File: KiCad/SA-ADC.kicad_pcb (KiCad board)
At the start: 4 copper layers, 99.1 x 94.2 mm, 226 parts, among them J1 Conn_01x03, J2 Conn_01x02, J3 Conn_01x08, SW1 SW_Push_SPDT, SW2 SW_Push, U1 40193, U10 74LVC1G32, U11 74LVC1G32, U12 74LVC1G32, U13 74LS21, U14 74LS21, U15 74LS21, U16 74LS21, U17 74LS21, U18 74AHC1G08, U19 74AHC1G08, U2 40193, U20 74LS21, U21 74AHC1G08, U22 74AHC1G08, U23 74LS21, U24 74LS21, U25 74AHC1G08, U26 74AHC1G08, U27 74AHC1G08, U28 74AHC1G08, U29 74LS21, U3 74HC04, U30 74LS21, U31 74AHC1G08, U32 74AHC1G08, U33 74AHC1G08, U34 LM358, U35 74LVC1G125, U36 74HC74, U37 LM317L_TO92, U38 L7805, U39 74HC74, U4 40245, U40 74HC74, U41 74HC74, U42 74LVC1G14, U43 74LS574, U44 LM555, U45 74LVC1G125, U46 74AHC1G08, U47 74LVC1G32, U48 74LVC1G125, U5 74LVC1G32, U6 74LVC1G32, U7 74LVC1G32, U8 74LVC1G32, U9 74LVC1G32

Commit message: Removed version nums
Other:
- board text added: "[version]"
- board text removed: "v0.0"
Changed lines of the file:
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@@
   (title_block
     (title SA-ADC)
-    (date 2020-02-13)
-    (rev "v0.0 (Prod.)")
   )
   (layers
@@
     (effects (font (size 2 2) (thickness 0.2)))
   )
-  (gr_text v0.0 (at 190.5 138.43) (layer B.SilkS)
+  (gr_text [version] (at 189.23 138.43) (layer B.SilkS)
     (effects (font (size 1 1) (thickness 0.15)) (justify mirror))
   )

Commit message: Fixed netlist-conformity due to renamed schematic sheet.
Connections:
- net /OutputDisplay/OUT_0 renamed Net-(J3-Pad1)
- net /OutputDisplay/OUT_1 renamed Net-(J3-Pad2)
- net /OutputDisplay/OUT_2 renamed Net-(J3-Pad3)
- net /OutputDisplay/OUT_3 renamed Net-(J3-Pad4)
- net /OutputDisplay/OUT_4 renamed Net-(J3-Pad5)
- net /OutputDisplay/OUT_5 renamed Net-(J3-Pad6)
- net /OutputDisplay/OUT_6 renamed Net-(J3-Pad7)
- net /OutputDisplay/OUT_7 renamed Net-(J3-Pad8)
- net /Registers.sch/Latch0 renamed /SA-Register.sch/Latch0
- net /Registers.sch/Latch1 renamed /SA-Register.sch/Latch1
- net /Registers.sch/Latch2 renamed /SA-Register.sch/Latch2
- net /Registers.sch/Latch3 renamed /SA-Register.sch/Latch3
- net /Registers.sch/Latch4 renamed /SA-Register.sch/Latch4
- net /Registers.sch/Latch5 renamed /SA-Register.sch/Latch5
- net /Registers.sch/Latch6 renamed /SA-Register.sch/Latch6
- net /Registers.sch/Latch7 renamed /SA-Register.sch/Latch7
- net /Registers.sch/LatchOutput renamed /Output/LatchOutput
- net /Registers.sch/Q0 renamed /Output/OUT_0
- net /Registers.sch/Q1 renamed /Output/OUT_1
- net /Registers.sch/Q2 renamed /Output/OUT_2
- net /Registers.sch/Q3 renamed /Output/OUT_3
- net /Registers.sch/Q4 renamed /Output/OUT_4
- net /Registers.sch/Q5 renamed /Output/OUT_5
- net /Registers.sch/Q6 renamed /Output/OUT_6
- net /Registers.sch/Q7 renamed /Output/OUT_7
- net /Registers.sch/Reset renamed /SA-Register.sch/Reset
- net /Registers.sch/Test0 renamed /SA-Register.sch/Test0
- net /Registers.sch/Test1 renamed /SA-Register.sch/Test1
- net /Registers.sch/Test2 renamed /SA-Register.sch/Test2
- net /Registers.sch/Test3 renamed /SA-Register.sch/Test3
- net /Registers.sch/Test4 renamed /SA-Register.sch/Test4
- net /Registers.sch/Test5 renamed /SA-Register.sch/Test5
- net /Registers.sch/Test6 renamed /SA-Register.sch/Test6
- net /Registers.sch/Test7 renamed /SA-Register.sch/Test7
- net /Registers.sch/~DFF_RST renamed /SA-Register.sch/~DFF_RST

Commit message: Fixed missing grounding on de-bounce cap
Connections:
- C54 pad 2: Net-(C54-Pad2) -> GND
- R60 pad 2: Net-(C54-Pad2) -> GND
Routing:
- net GND: track 508.7 -> 513.6 mm
- net Net-(C54-Pad2): track 1.91 -> 0.00 mm

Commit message: First part placement
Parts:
- removed C31, C32, C37, C42, C43, C44, C45, C51, C52: 0u1, Capacitor_SMD:C_0603_1608Metric
- removed D10, D11, D12, D13, D14, D15, D16, D17, D18, D44: LED_Small, LED_SMD:LED_0805_2012Metric
- removed R10, R11, R12, R13, R14, R15, R16, R17, R18, R68: rled, Resistor_SMD:R_0603_1608Metric
- removed R58: 10K, Resistor_SMD:R_0603_1608Metric
- removed U32, U33, U46: 74AHC1G08, Package_TO_SOT_SMD:SOT-353_SC-70-5
- removed U36, U39, U40, U41: 74HC74, Package_SO:TSSOP-14_4.4x5mm_P0.65mm
- removed U42: 74LVC1G14, Package_TO_SOT_SMD:SOT-353_SC-70-5
- removed U43: 74LS574, Package_SO:SOIC-20W_7.5x12.8mm_P1.27mm
- added H1: MountingHole, MountingHole:MountingHole_3.2mm_M3_Pad_Via, F.Cu at (99.1, 111.8)
- added H2: MountingHole, MountingHole:MountingHole_3.2mm_M3_Pad_Via, F.Cu at (186.1, 50.8)
- D1, D19, D2, D20, D21, D22, D23, D24, D25, D26, D27, D28, D29, D3, D30, D31, D32, D33, D34, D35, D36, D37, D38, D39, D4, D40, D41, D42, D43, D5, D6, D7, D8, D9: footprint LED_SMD:LED_0805_2012Metric -> LED_SMD:LED_0603_1608Metric
- JP1: value Jumper_NC_Small -> Conn_01x03; footprint Connector_PinHeader_2.54mm:PinHeader_1x02_P2.54mm_Vertical -> Connector_PinHeader_2.54mm:PinHeader_1x03_P2.54mm_Vertical
- U1: value 40193 -> 74LVC1G04; footprint Package_SO:TSSOP-16_4.4x5mm_P0.65mm -> Package_TO_SOT_SMD:SOT-353_SC-70-5
- U13, U14, U15, U16: value 74LS21 -> 74LVC1G32; footprint Package_SO:SOIC-14_3.9x8.7mm_P1.27mm -> Package_TO_SOT_SMD:SOT-353_SC-70-5
- U17, U20, U23: value 74LS21 -> 74LVC1G157; footprint Package_SO:SOIC-14_3.9x8.7mm_P1.27mm -> Package_TO_SOT_SMD:SOT-363_SC-70-6
- U18, U19, U21, U22: value 74AHC1G08 -> 74LVC1G157; footprint Package_TO_SOT_SMD:SOT-353_SC-70-5 -> Package_TO_SOT_SMD:SOT-363_SC-70-6
- U2: value 40193 -> 74LVC1G08; footprint Package_SO:TSSOP-16_4.4x5mm_P0.65mm -> Package_TO_SOT_SMD:SOT-353_SC-70-5
- U24: value 74LS21 -> 74LS377; footprint Package_SO:SOIC-14_3.9x8.7mm_P1.27mm -> Package_SO:SOIC-20W_7.5x12.8mm_P1.27mm
- U25, U27: value 74AHC1G08 -> 74LVC1G04
- U26: value 74AHC1G08 -> 74LS377; footprint Package_TO_SOT_SMD:SOT-353_SC-70-5 -> Package_SO:SOIC-20W_7.5x12.8mm_P1.27mm
- U28: value 74AHC1G08 -> 74HC164; footprint Package_TO_SOT_SMD:SOT-353_SC-70-5 -> Package_SO:SOIC-14_3.9x8.7mm_P1.27mm
- U29: value 74LS21 -> 74LVC1G175; footprint Package_SO:SOIC-14_3.9x8.7mm_P1.27mm -> Package_TO_SOT_SMD:SOT-363_SC-70-6
- U3: value 74HC04 -> 74LVC1G32; footprint Package_SO:SOIC-14_3.9x8.7mm_P1.27mm -> Package_TO_SOT_SMD:SOT-353_SC-70-5
- U30: value 74LS21 -> 74HC02
- U31: value 74AHC1G08 -> 74HC02; footprint Package_TO_SOT_SMD:SOT-353_SC-70-5 -> Package_SO:SOIC-14_3.9x8.7mm_P1.27mm
- U4: value 40245 -> 74HC245; footprint Package_SO:TSSOP-20_4.4x6.5mm_P0.65mm -> Package_SO:SSOP-20_5.3x7.2mm_P0.65mm
- moved R26 76.2 mm to (131.4, 54.6), turned to 90 degrees
- moved R25 75.8 mm to (133.3, 54.6), turned to 90 degrees
- moved R24 75.4 mm to (135.3, 54.6), turned to 90 degrees
- moved R23 75.2 mm to (137.2, 54.6), turned to 90 degrees
- moved R22 74.9 mm to (139.1, 54.6), turned to 90 degrees
- moved R21 74.7 mm to (141.0, 54.6), turned to 90 degrees
- moved R20 74.6 mm to (142.9, 54.6), turned to 90 degrees
- moved R19 74.5 mm to (144.8, 54.6), turned to 90 degrees
- moved D26 71.8 mm to (131.4, 61.0), turned to 90 degrees
- moved D25 71.4 mm to (133.3, 61.0), turned to 90 degrees
- moved D24 71.1 mm to (135.3, 61.0), turned to 90 degrees
- moved D23 70.8 mm to (137.2, 61.0), turned to 90 degrees
- moved D22 70.5 mm to (139.1, 61.0), turned to 90 degrees
- moved D21 70.3 mm to (141.0, 61.0), turned to 90 degrees
- moved D20 70.2 mm to (142.9, 61.0), turned to 90 degrees
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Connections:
- C17 pad 1: +5V -> GND
- C17 pad 2: GND -> +5V
- C18 pad 1: +5V -> GND
- C18 pad 2: GND -> +5V
- C2 pad 1: +5V -> GND
- C2 pad 2: GND -> +5V
- C20 pad 1: +5V -> GND
- C20 pad 2: GND -> +5V
- C21 pad 1: +5V -> GND
- C21 pad 2: GND -> +5V
- C25 pad 1: +5V -> GND
- C25 pad 2: GND -> +5V
- C28 pad 1: GND -> +5V
- C28 pad 2: +5V -> GND
- C29 pad 1: GND -> +5V
- C29 pad 2: +5V -> GND
- JP1 pad 1: +5V -> Net-(JP1-Pad1)
- R1 pad 2: /SA-Register.sch/Reset -> /SA-Register.sch/STATE_RST
- R2 pad 2: /Output/LatchOutput -> /SA-Register.sch/STATE0
- R3 pad 2: /SA-Register.sch/Test7 -> /SA-Register.sch/STATE1
- R4 pad 2: /SA-Register.sch/Latch7 -> /SA-Register.sch/STATE2
- R5 pad 2: /SA-Register.sch/Test6 -> /SA-Register.sch/STATE3
- R6 pad 2: /SA-Register.sch/Latch6 -> /SA-Register.sch/STATE4
- R60 pad 1: Net-(C54-Pad1) -> Net-(R59-Pad2)
- R7 pad 2: /SA-Register.sch/Test5 -> /SA-Register.sch/STATE5
- R8 pad 2: /SA-Register.sch/Latch5 -> /SA-Register.sch/STATE6
- R9 pad 2: /SA-Register.sch/Test4 -> /Analog/D7
- U1 pad 1: GND -> (no net)
- U1 pad 2: /StateMaschine.sch/Counter/C1 -> /SA-Register.sch/STATE_RST
- U1 pad 3: /StateMaschine.sch/Counter/C0 -> GND
- U1 pad 4: +5V -> Net-(U1-Pad4)
- U1 pad 5: /Clock/CLK -> +5V
- U10 pad 1: /SA-Register.sch/Test5 -> /SA-Register.sch/STATE5
- U11 pad 1: /SA-Register.sch/Test6 -> /SA-Register.sch/STATE6
- U12 pad 1: /SA-Register.sch/Test7 -> /SA-Register.sch/STATE2
- U12 pad 2: /Output/OUT_7 -> /SA-Register.sch/STATE_RST
- U12 pad 4: /Analog/D7 -> Net-(U12-Pad4)
- U13 pad 1: /StateMaschine.sch/StateDecode/~1 -> /SA-Register.sch/STATE3
- U13 pad 2: /StateMaschine.sch/StateDecode/~2 -> /SA-Register.sch/STATE_RST
- U13 pad 3: (no net) -> GND
- U13 pad 4: /StateMaschine.sch/StateDecode/~3 -> Net-(U13-Pad4)
- U13 pad 5: /StateMaschine.sch/StateDecode/~4 -> +5V
- U14 pad 1: /StateMaschine.sch/StateDecode/~1 -> /SA-Register.sch/STATE4
- U14 pad 2: /StateMaschine.sch/Counter/C2 -> /SA-Register.sch/STATE_RST
- U14 pad 3: (no net) -> GND
- U14 pad 4: /StateMaschine.sch/StateDecode/~3 -> Net-(U14-Pad4)
- U14 pad 5: /StateMaschine.sch/StateDecode/~4 -> +5V
- U15 pad 1: /StateMaschine.sch/StateDecode/~1 -> /SA-Register.sch/STATE5
- U15 pad 2: /StateMaschine.sch/StateDecode/~2 -> /SA-Register.sch/STATE_RST
- U15 pad 3: (no net) -> GND
- U15 pad 4: /StateMaschine.sch/Counter/C3 -> Net-(U15-Pad4)
- U15 pad 5: /StateMaschine.sch/StateDecode/~4 -> +5V
- U16 pad 1: /StateMaschine.sch/StateDecode/~1 -> /SA-Register.sch/STATE6
- U16 pad 2: /StateMaschine.sch/Counter/C2 -> /SA-Register.sch/STATE_RST
- U16 pad 3: (no net) -> GND
- U16 pad 4: /StateMaschine.sch/Counter/C3 -> Net-(U16-Pad4)
- U16 pad 5: /StateMaschine.sch/StateDecode/~4 -> +5V
- U17 pad 1: /StateMaschine.sch/Counter/C0 -> /Analog/COMP_OUT
- U17 pad 2: /StateMaschine.sch/Counter/C1 -> GND
- U17 pad 3: (no net) -> /Output/OUT_0
- U17 pad 4: /StateMaschine.sch/Counter/C2 -> Net-(U17-Pad4)
- U17 pad 5: /StateMaschine.sch/Counter/C3 -> +5V
- U17 pad 6: Net-(U17-Pad6) -> /SA-Register.sch/STATE0
- U18 pad 1: Net-(U17-Pad6) -> /SA-Register.sch/D
- U18 pad 2: /StateMaschine.sch/StateDecode/~4 -> GND
- U18 pad 3: GND -> /Output/OUT_1
- U18 pad 4: /SA-Register.sch/Latch0 -> Net-(U18-Pad4)
- U19 pad 1: Net-(U17-Pad8) -> /SA-Register.sch/D
- U19 pad 2: /StateMaschine.sch/StateDecode/~4 -> GND
- U19 pad 3: GND -> /Output/OUT_2
- U19 pad 4: /SA-Register.sch/Latch1 -> Net-(U19-Pad4)
- U2 pad 1: GND -> Net-(U1-Pad4)
- U2 pad 2: Net-(U2-Pad2) -> /Analog/COMP_OUT
- U2 pad 3: /StateMaschine.sch/Counter/C4 -> GND
- U2 pad 4: Net-(U1-Pad13) -> /SA-Register.sch/D
- U2 pad 5: Net-(U1-Pad12) -> +5V
- U20 pad 1: /StateMaschine.sch/Counter/C0 -> /SA-Register.sch/D
- U20 pad 2: /StateMaschine.sch/Counter/C1 -> GND
- U20 pad 3: (no net) -> /Output/OUT_3
- U20 pad 4: /StateMaschine.sch/StateDecode/~2 -> Net-(U20-Pad4)
- U20 pad 5: /StateMaschine.sch/Counter/C3 -> +5V
- U20 pad 6: Net-(U20-Pad6) -> Net-(U13-Pad4)
- U21 pad 1: Net-(U20-Pad6) -> /SA-Register.sch/D
- U21 pad 2: /StateMaschine.sch/StateDecode/~4 -> GND
- U21 pad 3: GND -> /Output/OUT_4
- U21 pad 4: /SA-Register.sch/Latch2 -> Net-(U21-Pad4)
- U22 pad 1: Net-(U20-Pad8) -> /SA-Register.sch/D
- U22 pad 2: /StateMaschine.sch/StateDecode/~4 -> GND
- U22 pad 3: GND -> /Output/OUT_5
- U22 pad 4: /SA-Register.sch/Latch3 -> Net-(U22-Pad4)
- U23 pad 1: /StateMaschine.sch/StateDecode/~0 -> /SA-Register.sch/D
- U23 pad 2: /StateMaschine.sch/StateDecode/~1 -> GND
- U23 pad 3: (no net) -> /Output/OUT_6
- U23 pad 4: /StateMaschine.sch/StateDecode/~2 -> Net-(U23-Pad4)
- U23 pad 5: /StateMaschine.sch/StateDecode/~3 -> +5V
- U23 pad 6: Net-(U23-Pad6) -> Net-(U16-Pad4)
- U24 pad 1: /StateMaschine.sch/Counter/C0 -> GND
- U24 pad 10: /StateMaschine.sch/StateDecode/~1 -> GND
- U24 pad 11: (no net) -> /Clock/CLK
- U24 pad 12: /StateMaschine.sch/Counter/C2 -> /Output/OUT_4
- U24 pad 13: /StateMaschine.sch/StateDecode/~3 -> Net-(U21-Pad4)
- U24 pad 14: +5V -> Net-(U22-Pad4)
- U24 pad 2: /StateMaschine.sch/Counter/C1 -> /Output/OUT_0
- U24 pad 3: (no net) -> Net-(U17-Pad4)
- U24 pad 4: /StateMaschine.sch/Counter/C2 -> Net-(U18-Pad4)
- U24 pad 5: /StateMaschine.sch/StateDecode/~3 -> /Output/OUT_1
- U24 pad 6: Net-(U24-Pad6) -> /Output/OUT_2
- U24 pad 7: GND -> Net-(U19-Pad4)
- U24 pad 8: Net-(U24-Pad8) -> Net-(U20-Pad4)
- U24 pad 9: /StateMaschine.sch/Counter/C0 -> /Output/OUT_3
- U25 pad 1: Net-(U23-Pad6) -> (no net)
- U25 pad 2: /StateMaschine.sch/Counter/C4 -> /Analog/D7
- U25 pad 4: /Output/LatchOutput -> Net-(U25-Pad4)
- U26 pad 1: Net-(U23-Pad8) -> Net-(U25-Pad4)
- U26 pad 2: /StateMaschine.sch/Counter/C4 -> Net-(J3-Pad1)
- U26 pad 3: GND -> /Output/OUT_0
- U26 pad 4: /SA-Register.sch/Reset -> /Output/OUT_1
- U26 pad 5: +5V -> Net-(J3-Pad2)
- U27 pad 1: Net-(U24-Pad6) -> (no net)
- U27 pad 2: /StateMaschine.sch/StateDecode/~4 -> /Clock/CLK
- U27 pad 4: /SA-Register.sch/Latch4 -> Net-(U27-Pad4)
- U28 pad 1: Net-(U24-Pad8) -> /StateMaschine.sch/C_IN
- U28 pad 2: /StateMaschine.sch/StateDecode/~4 -> /StateMaschine.sch/C_IN
- U28 pad 3: GND -> /SA-Register.sch/STATE_RST
- U28 pad 4: /SA-Register.sch/Latch5 -> /SA-Register.sch/STATE0
- U28 pad 5: +5V -> /SA-Register.sch/STATE1
- U29 pad 1: /StateMaschine.sch/Counter/C0 -> Net-(U27-Pad4)
- U29 pad 2: /StateMaschine.sch/Counter/C1 -> GND
- U29 pad 3: (no net) -> /SA-Register.sch/STATE6
- U29 pad 4: /StateMaschine.sch/StateDecode/~2 -> /Analog/D7
- U29 pad 5: /StateMaschine.sch/StateDecode/~3 -> +5V
- U29 pad 6: Net-(U29-Pad6) -> +5V
- U3 pad 1: /StateMaschine.sch/Counter/C0 -> /SA-Register.sch/STATE1
- U3 pad 2: /StateMaschine.sch/StateDecode/~0 -> /SA-Register.sch/STATE_RST
- U3 pad 3: /StateMaschine.sch/Counter/C1 -> GND
- U3 pad 4: /StateMaschine.sch/StateDecode/~1 -> Net-(U18-Pad6)
- U3 pad 5: /StateMaschine.sch/Counter/C2 -> +5V
- U30 pad 1: /StateMaschine.sch/StateDecode/~0 -> Net-(U30-Pad1)
- U30 pad 10: GND -> Net-(U30-Pad10)
- U30 pad 11: (no net) -> /SA-Register.sch/STATE5
- U30 pad 12: GND -> /SA-Register.sch/STATE6
- U30 pad 13: GND -> Net-(U30-Pad13)
- U30 pad 2: /StateMaschine.sch/Counter/C1 -> /SA-Register.sch/STATE_RST
- U30 pad 3: (no net) -> /SA-Register.sch/STATE0
- U30 pad 4: /StateMaschine.sch/StateDecode/~2 -> Net-(U30-Pad4)
- U30 pad 5: /StateMaschine.sch/StateDecode/~3 -> /SA-Register.sch/STATE1
- U30 pad 6: Net-(U30-Pad6) -> /SA-Register.sch/STATE2
- U30 pad 8: Net-(U30-Pad8) -> /SA-Register.sch/STATE3
- U30 pad 9: GND -> /SA-Register.sch/STATE4
- U31 pad 1: Net-(U29-Pad6) -> Net-(U31-Pad1)
- U31 pad 2: /StateMaschine.sch/StateDecode/~4 -> Net-(U30-Pad1)
- U31 pad 3: GND -> Net-(U30-Pad4)
- U31 pad 4: /SA-Register.sch/Latch6 -> Net-(U31-Pad4)
- U31 pad 5: +5V -> Net-(U30-Pad10)
- U4 pad 1: GND -> +5V
- U4 pad 11: /Analog/D0 -> /Analog/DAC/D7
- U4 pad 12: /Analog/D1 -> /Analog/DAC/D6
- U4 pad 13: /Analog/D2 -> /Analog/DAC/D5
- U4 pad 14: /Analog/D3 -> /Analog/DAC/D4
- U4 pad 15: /Analog/D4 -> /Analog/DAC/D3
- U4 pad 16: /Analog/D5 -> /Analog/DAC/D2
- U4 pad 17: /Analog/D6 -> /Analog/DAC/D1
- U4 pad 18: /Analog/D7 -> /Analog/DAC/D0
- U4 pad 2: /Analog/DAC/D7 -> /Analog/D0
- U4 pad 3: /Analog/DAC/D6 -> /Analog/D1
- U4 pad 4: /Analog/DAC/D5 -> /Analog/D2
- U4 pad 5: /Analog/DAC/D4 -> /Analog/D3
- U4 pad 6: /Analog/DAC/D3 -> /Analog/D4
- U4 pad 7: /Analog/DAC/D2 -> /Analog/D5
- U4 pad 8: /Analog/DAC/D1 -> /Analog/D6
- U4 pad 9: /Analog/DAC/D0 -> /Analog/D7
- U45 pad 4: Net-(U45-Pad4) -> Net-(JP1-Pad1)
- U47 pad 1: Net-(U46-Pad4) -> Net-(JP1-Pad2)
- U5 pad 1: /SA-Register.sch/Test0 -> /SA-Register.sch/STATE0
- U6 pad 1: /SA-Register.sch/Test1 -> /SA-Register.sch/STATE1
- U7 pad 1: /SA-Register.sch/Test2 -> /SA-Register.sch/STATE2
- U8 pad 1: /SA-Register.sch/Test3 -> /SA-Register.sch/STATE3
- U9 pad 1: /SA-Register.sch/Test4 -> /SA-Register.sch/STATE4
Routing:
- net GND: track 513.6 -> 0.00 mm, vias 120 -> 0
- net +5V: track 259.7 -> 0.00 mm, vias 58 -> 0
- net /StateMaschine.sch/StateDecode/~4: track 179.4 -> 0.00 mm, vias 18 -> 0
- net /StateMaschine.sch/Counter/C0: track 150.9 -> 0.00 mm, vias 14 -> 0
- net /StateMaschine.sch/StateDecode/~1: track 149.8 -> 0.00 mm, vias 11 -> 0
- net /StateMaschine.sch/Counter/C1: track 144.6 -> 0.00 mm, vias 9 -> 0
- net /SA-Register.sch/Test0: track 131.3 -> 0.00 mm, vias 8 -> 0
- net /StateMaschine.sch/StateDecode/~2: track 130.9 -> 0.00 mm, vias 12 -> 0
- net /Analog/COMP_OUT: track 128.6 -> 0.00 mm, vias 4 -> 0
- net /StateMaschine.sch/StateDecode/~3: track 124.3 -> 0.00 mm, vias 13 -> 0
- net /SA-Register.sch/Test1: track 122.1 -> 0.00 mm, vias 6 -> 0
- net /Output/LatchOutput: track 121.1 -> 0.00 mm, vias 4 -> 0
- net /SA-Register.sch/Test3: track 112.0 -> 0.00 mm, vias 6 -> 0
- net VDDA: track 105.4 -> 0.00 mm, vias 4 -> 0
- net /Output/OUT_2: track 104.0 -> 0.00 mm, vias 5 -> 0
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- removed copper zone on In2.Cu, net +5V
- removed copper zone on In1.Cu, net GND
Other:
- board size 99.1 x 94.2 mm -> 95.9 x 69.2 mm
- board text added: "ON-OFF"
- board text added: "OUT"
- board text added: "Output"
- board text added: "R"
- board text added: "STEP"
- board text added: "StateM."
- board text removed: "1"
- board text removed: "2"
- board text removed: "3"
- board text removed: "4"
- board text removed: "5"
- board text removed: "6"
- board text removed: "Clock EN"
- board text removed: "DAC VALUE"
- board text removed: "Latch"
- board text removed: "OUTPUT"
- board text removed: "Outp."
- board text removed: "Reset"
- board text removed: "Set"
- board text removed: "State Machine"
- board text removed: "Successive-Approximation Register"
- board text removed: "Test"
- board text removed: "Value Stored:"

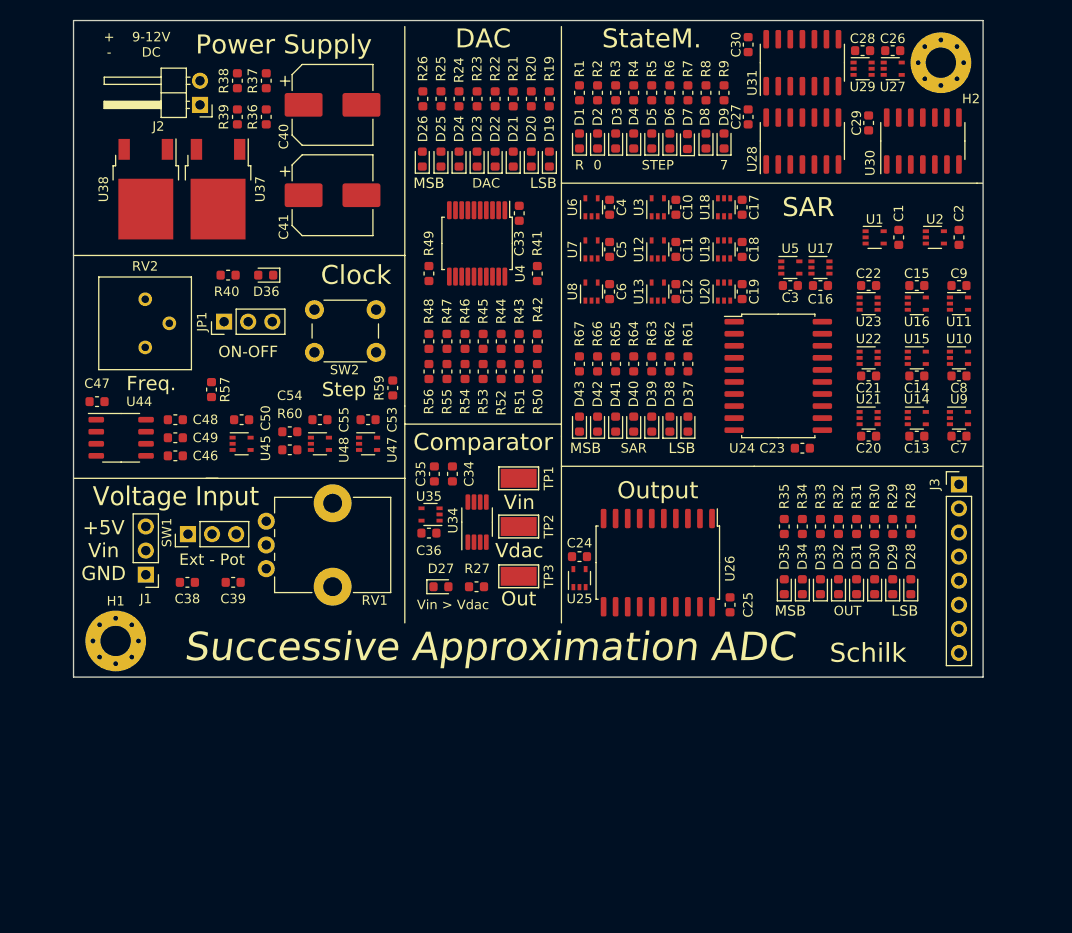
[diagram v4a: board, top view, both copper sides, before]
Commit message: First Layout (All Connected, passes DRC)
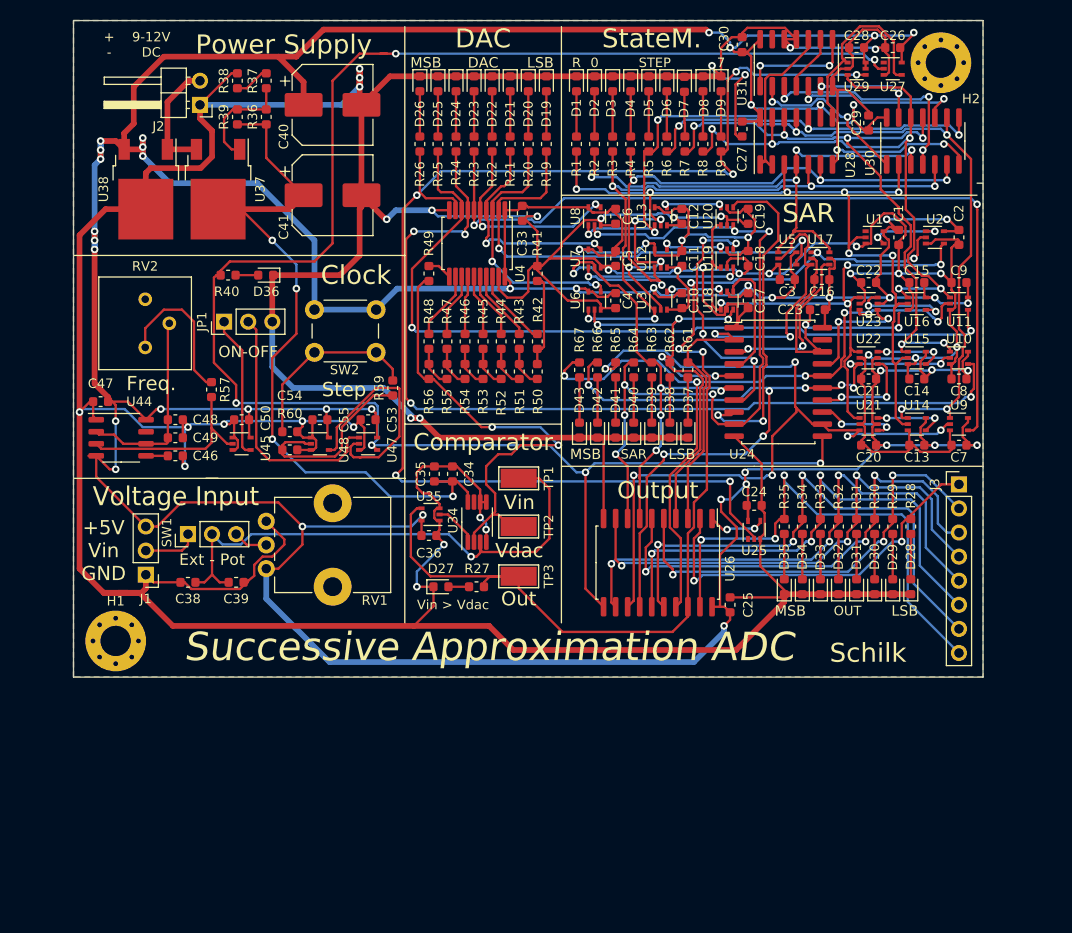
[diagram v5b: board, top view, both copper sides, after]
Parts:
- moved C24 19.2 mm to (166.4, 97.5)
- moved U25 19.1 mm to (166.4, 100.1)
- moved C23 14.7 mm to (173.0, 76.8), turned to 0 degrees
- moved C17 9.86 mm to (165.7, 75.9)
- moved C10 9.86 mm to (158.8, 75.9)
- moved C4 9.86 mm to (151.8, 75.9)
- moved U18 9.85 mm to (163.5, 75.9)
- moved U3 9.85 mm to (156.5, 75.9)
- moved U6 9.85 mm to (149.5, 75.9)
- moved C19 7.96 mm to (165.7, 67.0)
- moved C12 7.96 mm to (158.8, 67.0)
- moved C6 7.96 mm to (151.8, 67.0)
- moved D19 7.94 mm to (144.5, 53.0), turned to 270 degrees
- moved D20 7.94 mm to (142.6, 53.0), turned to 270 degrees
- moved D21 7.94 mm to (140.7, 53.0), turned to 270 degrees
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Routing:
- net GND: track 0.00 -> 830.1 mm, vias 0 -> 41
- net +5V: track 0.00 -> 659.7 mm, vias 0 -> 49
- net /Clock/CLK: track 0.00 -> 193.6 mm, vias 0 -> 6
- net /Analog/D7: track 0.00 -> 143.8 mm, vias 0 -> 6
- net /Analog/COMP_OUT: track 0.00 -> 112.7 mm, vias 0 -> 5
- net /SA-Register.sch/STATE_RST: track 0.00 -> 104.3 mm, vias 0 -> 11
- net /Analog/D5: track 0.00 -> 97.6 mm, vias 0 -> 4
- net /Analog/D4: track 0.00 -> 87.1 mm, vias 0 -> 2
- net /Output/OUT_4: track 0.00 -> 85.8 mm, vias 0 -> 6
- net /Analog/D6: track 0.00 -> 84.6 mm, vias 0 -> 2
- net /Output/OUT_5: track 0.00 -> 81.0 mm, vias 0 -> 9
- net /Output/OUT_6: track 0.00 -> 80.4 mm, vias 0 -> 6
- net VDDA: track 0.00 -> 80.1 mm, vias 0 -> 4
- net /Output/OUT_3: track 0.00 -> 76.4 mm, vias 0 -> 7
- net /SA-Register.sch/STATE4: track 0.00 -> 76.0 mm, vias 0 -> 5
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- added copper zone on B.Cu, net +5V
- added copper zone on F.Cu, net GND
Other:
- copper layers 4 -> 2

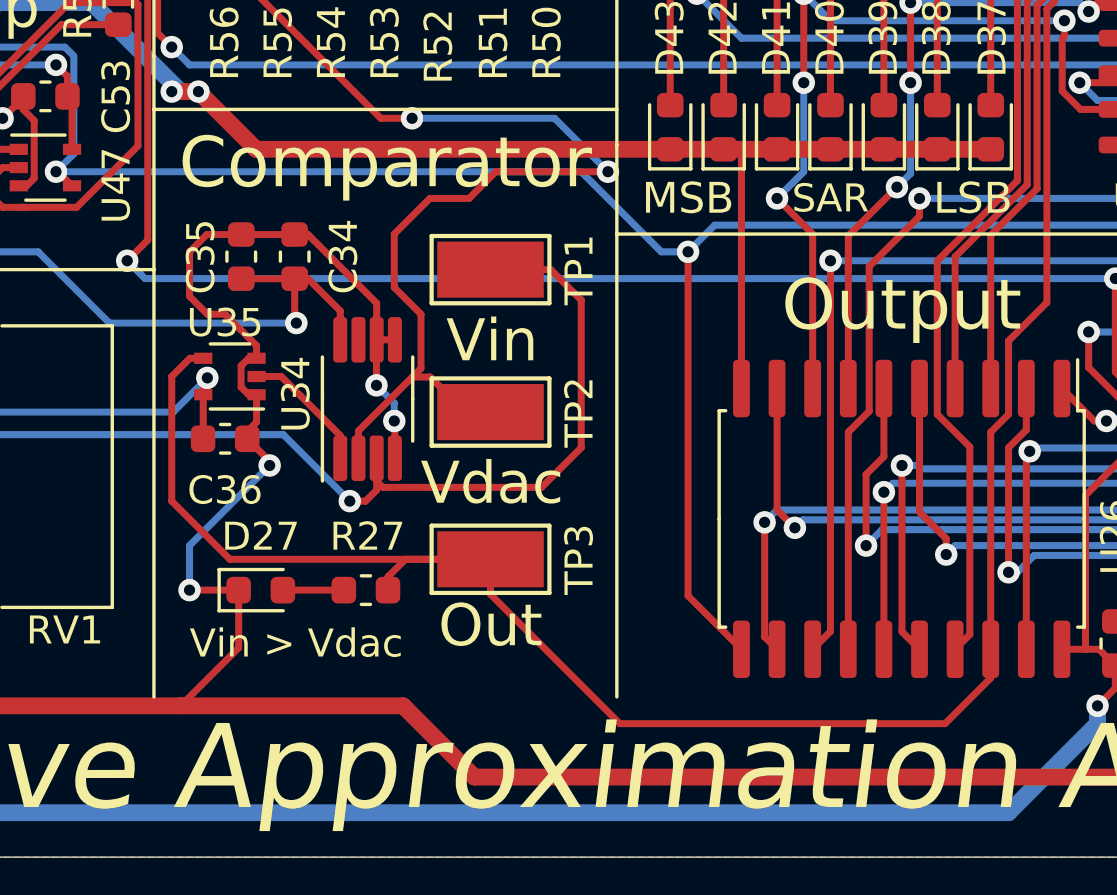
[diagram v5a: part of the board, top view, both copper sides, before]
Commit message: Added GND test-point
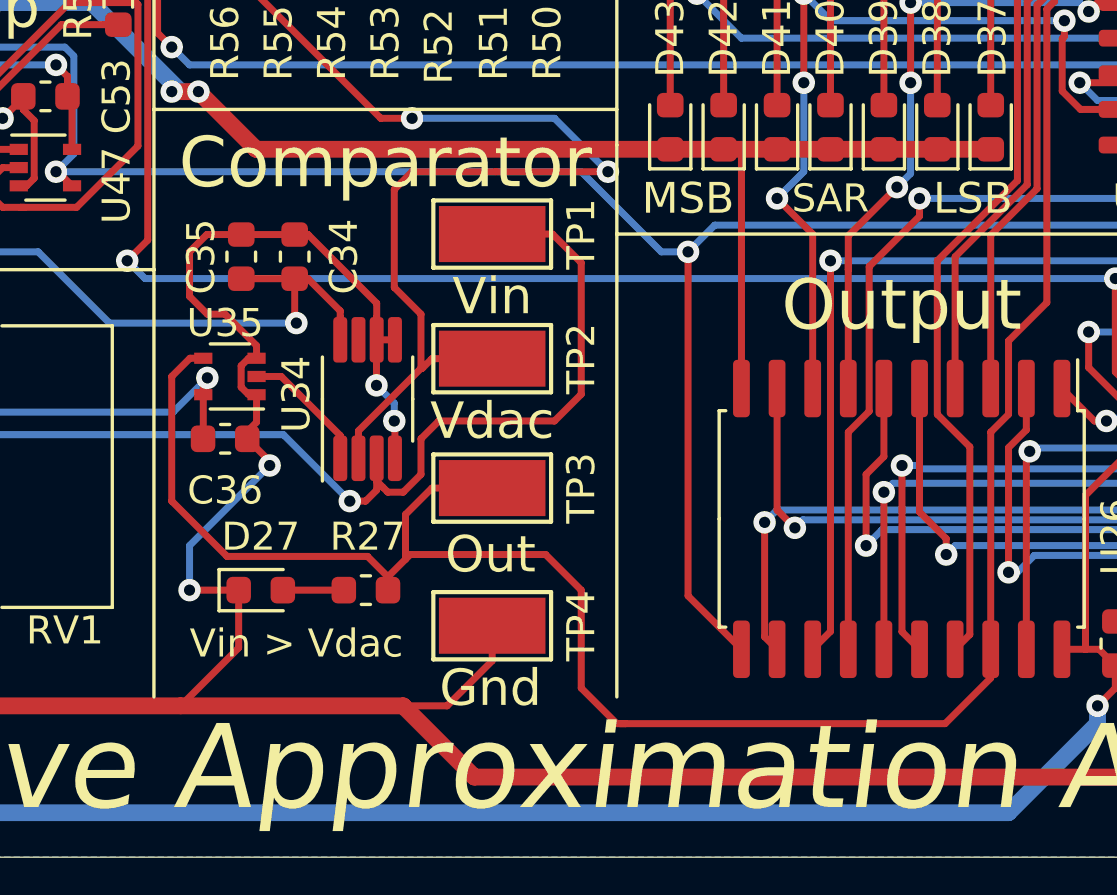
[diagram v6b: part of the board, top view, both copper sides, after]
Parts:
- added TP4: GND, TestPoint:TestPoint_Keystone_5019_Minature, F.Cu at (141.6, 107.3)
- moved TP3 2.54 mm to (141.6, 102.4)
- moved TP2 1.91 mm to (141.6, 97.8)
- moved TP1 1.27 mm to (141.6, 93.3)
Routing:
- net GND: track 830.1 -> 835.2 mm
- net /Analog/COMP_OUT: track 112.7 -> 116.1 mm
- net /Input/VIN: track 56.8 -> 57.8 mm
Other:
- board text added: "Gnd"
